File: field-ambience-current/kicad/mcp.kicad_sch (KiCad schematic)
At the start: 45 parts, among them SW1 Cell 1 (2u Choc V2 Hot-Swap), SW10 Modifier CLEAR (12x12x7.3 SMD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, SW2 Cell 2 (2u Choc V2 Hot-Swap), SW3 Cell 3 (2u Choc V2 Hot-Swap), SW4 Cell 4 (2u Choc V2 Hot-Swap), SW5 Cell 5 (2u Choc V2 Hot-Swap), SW6 Modifier SHIFT (12x12x7.3 SMD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, SW7 Modifier HOLD (12x12x7.3 SMD-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, SW8 Modifier DRONE (12x12x7.3 SMD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, SW9 Modifier GENERATE (12x12x7.3 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

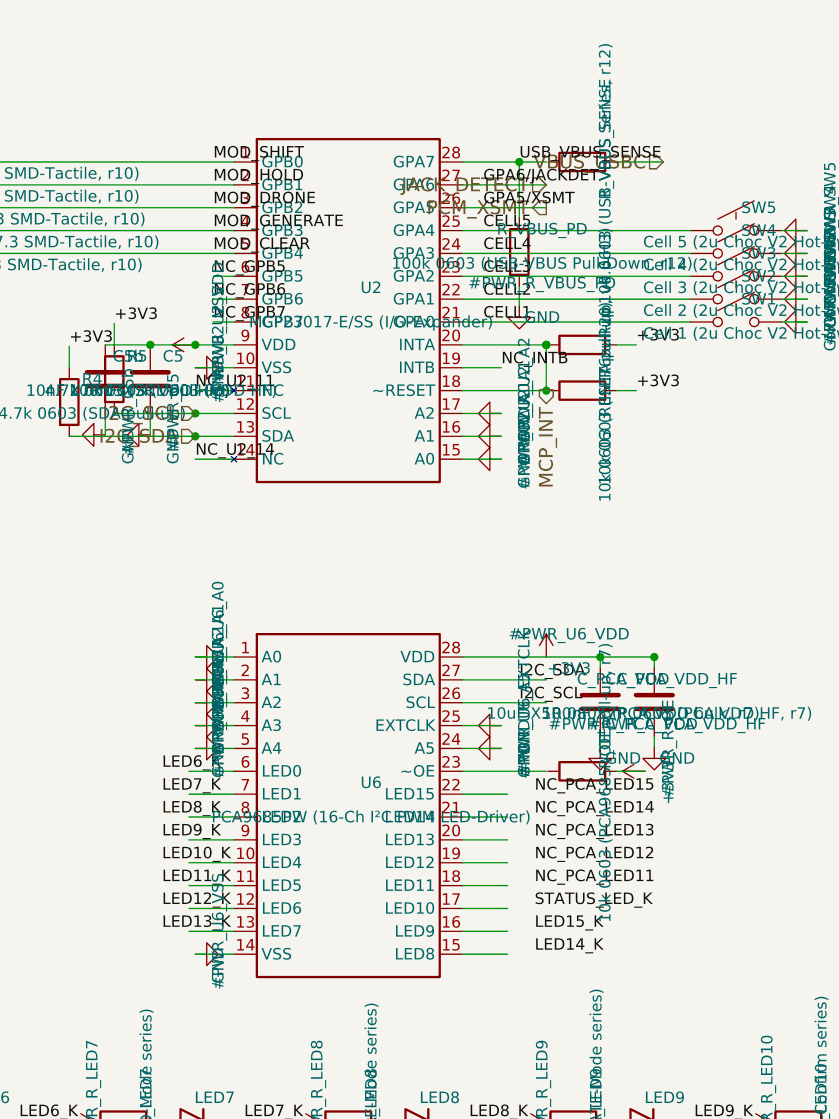
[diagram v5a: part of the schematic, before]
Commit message: pcb(gen): kicad-Analyzer-Bugfixes (ERC: 8 errors→6, NT-001 33→16)
Schematic-Analyzer fand drei klassen von echten Connectivity-Bugs in den
beiden Generator-Catchup-Commits (50b5e02 + 0a3a740). Alle gefixt.

Bug 1: Label-Position 3mm neben Wire-Endpunkt → 33 dangling-pin-Nets
  - r10-LED PCA-pin-Labels (10 LEDs + 5 NC + STATUS_LED_K) saßen bei
    PCA_PIN_*_X±8 statt ±5 → keine 10 LEDs waren physisch an PCA9685
    connected. Fix: Labels auf Wire-Endpunkt verschoben.

Bug 2: Sub-mm-Gaps (0.19mm) zwischen Wires und Resistor-Pins
  - R rotation=90 horizontal hat pin1/pin2 bei sx±3.81 (X.19/X.81).
    Meine Wires endeten bei integer-mm → 0.19mm Gap = dangling.
  - Fixed: R_OE (mcp_sheet PCA-OE), R_VBUS_SENSE (mcp_sheet GPA7),
    R_CHRG (battery_sheet U7-STAT), R21 (battery_sheet U7-PROG).

Bug 3: Y-Inversion bei Q1 DMG2305UX P-MOS
  - KiCad-Symbol-local-Y ist invertiert zu Schematic-abs-Y. Meine
    q1_s_y und q1_d_y waren vertauscht → Q1.2 (S) auf +5V_OUT statt
    VBUS_USBC (SPEC-§2.2-violation!). Analyzer hat das korrekt
    gefangen. Fix: Y-Werte getauscht, S=VBUS_USBC ✓, D=+5V_OUT ✓.

Bug 4: Lokal-Label statt Hier-Label für Cross-Sheet-Nets
  - Lokale Labels mergen NICHT mit Hier-Labels im Analyzer-View
    (auch wenn KiCad-GUI das toleriert). Battery_sheet U7-VDD,
    U7-VBAT, U8-VIN, L1-top, Q1-D, D3-K, J9-pin1, C_BAT_IN waren
    alle mit lokalen Labels markiert → keine Cross-Sheet-Merge.
    Plus mcp_sheet PCA-side I²C-SCL/SDA.
  - Fix: alle zu hier_labels umgewandelt. I²C-Bus hat jetzt 4 Pins
    (U1+U2+R-Pullup+U6) statt 2 isolierte Sub-Nets.

Bug 5: +5V_OUT (Battery) mergt nicht mit System +5V
  - Hier-Label-Name "+5V_OUT" ≠ Power-Tree-Net-Name "+5V". Battery's
    +5V_OUT war ein isoliertes 2-pin Net (D3.K + Q1.D).
  - Fix: Bridge-Label "+5V_OUT" am existing Power-Tree→Pico-Wire
    (110, 50) im root_sheet. +5V hat jetzt 49 pins (war 47).

Bug 6: Redundante Edge-Hier-Labels in battery_sheet
  - Hatte standalone hier_labels bei (235, 70/80) zusätzlich zu de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
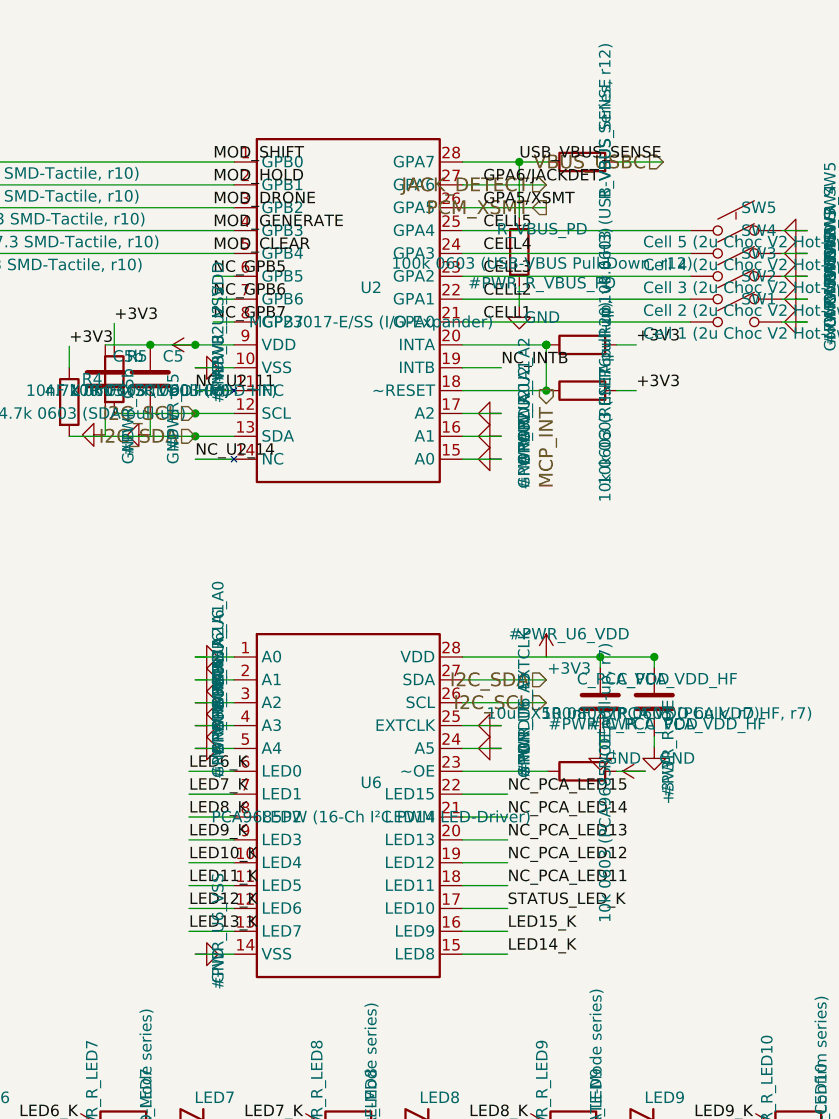
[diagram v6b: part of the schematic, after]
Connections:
- net LED10_K: now also U6.10 (LED4)
- net LED11_K: now also U6.11 (LED5)
- net LED12_K: now also U6.12 (LED6)
- net LED13_K: now also U6.13 (LED7)
- net LED14_K: now also U6.15 (LED8)
- net LED15_K: now also U6.16 (LED9)
- net LED6_K: now also U6.6 (LED0)
- net LED7_K: now also U6.7 (LED1)
- net LED8_K: now also U6.8 (LED2)
- net LED9_K: now also U6.9 (LED3)
- net NC_PCA_LED11: now also U6.18 (LED11)
- net NC_PCA_LED12: now also U6.19 (LED12)
- net NC_PCA_LED13: now also U6.20 (LED13)
- net NC_PCA_LED14: now also U6.21 (LED14)
- net NC_PCA_LED15: now also U6.22 (LED15)
- net STATUS_LED_K: now also U6.17 (LED10)
- net USB_VBUS_SENSE: now also R_VBUS_SENSE.1
- net at R_OE.1: now also U6.23 (~OE)
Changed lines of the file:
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@@
     (stroke (width 0) (type default))
 )
-  (wire (pts (xy 142.7 93.49) (xy 152 93.49))
+  (wire (pts (xy 142.7 93.49) (xy 152.19 93.49))
     (stroke (width 0) (type default))
 )
@@
     (stroke (width 0) (type default))
 )
-  (wire (pts (xy 142.7 161.19) (xy 152 161.19))
+  (wire (pts (xy 142.7 161.19) (xy 152.19 161.19))
     (stroke (width 0) (type default))
 )
@@
     (effects (font (size 1.27 1.27)) (justify left bottom))
 )
-  (label "I2C_SDA" (at 149 151.03 0) (fields_autoplaced)
-    (effects (font (size 1.27 1.27)) (justify left bottom))
-)
-  (label "I2C_SCL" (at 149 153.57000000000002 0) (fields_autoplaced)
-    (effects (font (size 1.27 1.27)) (justify left bottom))
-)
   (label "LED6_K" (at 93.43 200 0) (fields_autoplaced)
     (effects (font (size 1.27 1.27)) (justify left bottom))
 )
-  (label "LED6_K" (at 109.3 161.19 0) (fields_autoplaced)
+  (label "LED6_K" (at 112.3 161.19 0) (fields_autoplaced)
     (effects (font (size 1.27 1.27)) (justify left bottom))
 )
@@
     (effects (font (size 1.27 1.27)) (justify left bottom))
 )
-  (label "LED7_K" (at 109.3 163.73000000000002 0) (fields_autoplaced)
+  (label "LED7_K" (at 112.3 163.73000000000002 0) (fields_autoplaced)
     (effects (font (size 1.27 1.27)) (justify left bottom))
 )
@@
     (effects (font (size 1.27 1.27)) (justify left bottom))
 )
-  (label "LED8_K" (at 109.3 166.27 0) (fields_autoplaced)
+  (label "LED8_K" (at 112.3 166.27 0) (fields_autoplaced)
     (effects (font (size 1.27 1.27)) (justify left bottom))
 )
@@
     (effects (font (size 1.27 1.27)) (justify left bottom))
 )
-  (label "LED9_K" (at 109.3 168.81 0) (fields_autoplaced)
+  (label "LED9_K" (at 112.3 168.81 0) (fields_autoplaced)
     (effects (font (size 1.27 1.27)) (justify left bottom))
 )
@@
     (effects (font (size 1.27 1.27)) (justify left bottom))
 )
-  (label "LED10_K" (at 109.3 171.35000000000002 0) (fields_autoplaced)
+  (label "LED10_K" (at 112.3 171.35000000000002 0) (fields_autoplaced)
     (effects (font (size 1.27 1.27)) (justify left bottom))
 )
@@
     (effects (font (size 1.27 1.27)) (justify left bottom))
 )
-  (label "LED11_K" (at 109.3 173.89000000000001 0) (fields_autoplaced)
+  (label "LED11_K" (at 112.3 173.89000000000001 0) (fields_autoplaced)
     (effects (font (size 1.27 1.27)) (justify left bottom))
 )
@@
     (effects (font (size 1.27 1.27)) (justify left bottom))
 )
-  (label "LED12_K" (at 109.3 176.43 0) (fields_autoplaced)
+  (label "LED12_K" (at 112.3 176.43 0) (fields_autoplaced)
     (effects (font (size 1.27 1.27)) (justify left bottom))
 )
@@
     (effects (font (size 1.27 1.27)) (justify left bottom))
 )
-  (label "LED13_K" (at 109.3 178.97 0) (fields_autoplaced)
+  (label "LED13_K" (at 112.3 178.97 0) (fields_autoplaced)
     (effects (font (size 1.27 1.27)) (justify left bottom))
 )
@@
     (effects (font (size 1.27 1.27)) (justify left bottom))
 )
-  (label "LED14_K" (at 150.7 181.51000000000002 0) (fields_autoplaced)
+  (label "LED14_K" (at 147.7 181.51000000000002 0) (fields_autoplaced)
     (effects (font (size 1.27 1.27)) (justify left bottom))
 )
@@
     (effects (font (size 1.27 1.27)) (justify left bottom))
 )
-  (label "LED15_K" (at 150.7 178.97 0) (fields_autoplaced)
-    (effects (font (size 1.27 1.27)) (justify left bottom))
-)
-  (label "STATUS_LED_K" (at 150.7 176.43 0) (fields_autoplaced)
-    (effects (font (size 1.27 1.27)) (justify left bottom))
-)
-  (label "NC_PCA_LED11" (at 150.7 173.89000000000001 0) (fields_autoplaced)
-    (effects (font (size 1.27 1.27)) (justify left bottom))
-)
-  (label "NC_PCA_LED12" (at 150.7 171.35000000000002 0) (fields_autoplaced)
-    (effects (font (size 1.27 1.27)) (justify left bottom))
-)
-  (label "NC_PCA_LED13" (at 150.7 168.81 0) (fields_autoplaced)
-    (effects (font (size 1.27 1.27)) (justify left bottom))
-)
-  (label "NC_PCA_LED14" (at 150.7 166.27 0) (fields_autoplaced)
-    (effects (font (size 1.27 1.27)) (justify left bottom))
-)
-  (label "NC_PCA_LED15" (at 150.7 163.73000000000002 0) (fields_autoplaced)
+  (label "LED15_K" (at 147.7 178.97 0) (fields_autoplaced)
+    (effects (font (size 1.27 1.27)) (justify left bottom))
+)
+  (label "STATUS_LED_K" (at 147.7 176.43 0) (fields_autoplaced)
+    (effects (font (size 1.27 1.27)) (justify left bottom))
+)
+  (label "NC_PCA_LED11" (at 147.7 173.89000000000001 0) (fields_autoplaced)
+    (effects (font (size 1.27 1.27)) (justify left bottom))
+)
+  (label "NC_PCA_LED12" (at 147.7 171.35000000000002 0) (fields_autoplaced)
+    (effects (font (size 1.27 1.27)) (justify left bottom))
+)
+  (label "NC_PCA_LED13" (at 147.7 168.81 0) (fields_autoplaced)
+    (effects (font (size 1.27 1.27)) (justify left bottom))
+)
+  (label "NC_PCA_LED14" (at 147.7 166.27 0) (fields_autoplaced)
+    (effects (font (size 1.27 1.27)) (justify left bottom))
+)
+  (label "NC_PCA_LED15" (at 147.7 163.73000000000002 0) (fields_autoplaced)
     (effects (font (size 1.27 1.27)) (justify left bottom))
 )
@@
     (effects (font (size 1.524 1.524)) (justify right))
 )
+  (hierarchical_label "I2C_SDA" (shape input) (at 152 151.03 0)
+    (effects (font (size 1.524 1.524)) (justify right))
+)
+  (hierarchical_label "I2C_SCL" (shape input) (at 152 153.57000000000002 0)
+    (effects (font (size 1.524 1.524)) (justify right))
+)
